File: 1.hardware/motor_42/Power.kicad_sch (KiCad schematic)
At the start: 0 parts

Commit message: 중간 저장
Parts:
- added C1: 10uF/50V, symbol Device:C_Small_US
- added C17, C18, C19, C20: CL31A106KBHNNNE, symbol Device:C_Small_US
- added C2, C3, C9: 0.1uF/50V, symbol Device:C_Small_US
- added C4, C5, C7, C8: 22uF/16V, symbol Device:C_Small_US
- added C6: 75pF/50V, symbol Device:C_Small_US
- added D1: SS54F-HF, SODFL4626X120N, symbol SamacSys_Parts:SS54F-HF
- added D2: SMBJ28CA-Q, DIONM5436X244N, symbol SamacSys_Parts:SMBJ28CA-Q
- added D3: B5819WS, SOD2613X100N, symbol SamacSys_Parts:B5819WS
- added H1, H2, H3, H4: MountingHole, symbol Mechanical:MountingHole
- added L1: 15uH, symbol Device:L
- added L2: 2.2uH, symbol Device:L
- added PS1: TPS563201DDCT, SOT95P280X110-6N, symbol SamacSys_Parts:TPS563201DDCT
- added R1: 100k/0.063w, symbol Device:R_Small_US
- added R2: 13.3k/0.063w, symbol Device:R_Small_US
- added R3: 511k/0.063w, symbol Device:R_Small_US
- added R4: 105k/0.063w, symbol Device:R_Small_US
- added R5: 49.9R/0.063w, symbol Device:R_Small_US
- added R6, R8: 10k/0.063w, symbol Device:R_Small_US
- added R7: 33.2k/0.063w, symbol Device:R_Small_US
- added U3: TPS54202DDC, Package_TO_SOT_SMD:SOT-23-6, symbol Regulator_Switching:TPS54202DDC
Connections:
- net GND: now also C1.2, C17.2, C18.2, C19.2, C2.2, C20.2, C4.2, C5.2, C7.2, C8.2, D2.2, PS1.1 (GND), R2.2, R4.2, R6.2, U3.1 (GND)
- net VCC: now also C17.1, C18.1, C19.1, C20.1, D1.1, D2.1, D3.2
- new net: C1.1, C2.1, D3.1, R3.1, U3.3 (VIN)
- new net: C3.2, L1.1, U3.2 (SW)
- new net: C9.2, L2.2, PS1.2 (SW)
- new net: PS1.4 (VFB), R6.1, R7.2
- new net: C9.1, PS1.6 (VBST)
- new net: R3.2, R4.1, U3.5 (EN)
- new net: C6.1, R1.1, R5.2
- new net: C6.2, R1.2, R2.1, U3.4 (FB)
- new net: PS1.5 (EN), R8.1
- new net: C3.1, U3.6 (BOOT)
- new net 3V3: C7.1, C8.1, L2.1, R7.1
- new net 5V: C4.1, C5.1, L1.2, PS1.3 (VIN), R5.1, R8.2
- new net VCC_IN: D1.2
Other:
- note added: "3V3"
- note added: "5V"

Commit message: 중간 저장
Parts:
- renumbered C17 to C1, C6 to C10, C9 to C11, C7 to C12, C8 to C13, C18 to C2, C19 to C3, C20 to C4, C3 to C5, C1 to C6, C2 to C7, C4 to C8, C5 to C9, R3 to R1, R5 to R2, R1 to R3, R2 to R5, R7 to R6, R8 to R7, R6 to R8, U3 to U1

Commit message: 회로도 대충 완성
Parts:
- removed D1: SS54F-HF, SODFL4626X120N, symbol SamacSys_Parts:SS54F-HF
- removed D2: SMBJ28CA-Q, DIONM5436X244N, symbol SamacSys_Parts:SMBJ28CA-Q
- added D2: SMBJ28CAQ-13-F, SamacSys_Parts:DIONM5336X250N, symbol SamacSys_Parts:SMBJ28CAQ-13-F
- added D5: SS54, PCM_Diode_SMD_AKL:D_SMC, symbol PCM_Diode_Schottky_AKL:SS54
- added J10: Conn_01x02, symbol Connector_Generic:Conn_01x02
- D3: footprint SOD2613X100N -> Diode_SMD:D_SOD-323
- H1, H2, H3, H4: footprint (none) -> MountingHole:MountingHole_3.2mm_M3
- R1: footprint (none) -> Resistor_SMD:R_0402_1005Metric
- R2: renamed from R4; footprint (none) -> Resistor_SMD:R_0402_1005Metric
- R3: renamed from R7; footprint (none) -> Resistor_SMD:R_0402_1005Metric
- R4: renamed from R6; footprint (none) -> Resistor_SMD:R_0402_1005Metric
- R5: renamed from R8; footprint (none) -> Resistor_SMD:R_0402_1005Metric
- R6: renamed from R2; footprint (none) -> Resistor_SMD:R_0402_1005Metric
- R7: renamed from R3; footprint (none) -> Resistor_SMD:R_0402_1005Metric
- R8: renamed from R5; footprint (none) -> Resistor_SMD:R_0402_1005Metric
- renumbered C12 to C1, C4 to C10, C8 to C11, C9 to C12, C10 to C13, C6 to C2, C13 to C3, C7 to C4, C11 to C5, C1 to C6, C2 to C7, C3 to C8, C5 to C9, L2 to L1, L1 to L2
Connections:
- net 5V: now also J10.1 (Pin_1)
- net GND: now also D2.2
- net VCC: now also D2.1, D5.1 (K)
- net VCC_IN: now also D5.2 (A)
- new net USB_VBUS: J10.2 (Pin_2)

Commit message: 수정
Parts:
- removed PS1: TPS563201DDCT, SOT95P280X110-6N, symbol SamacSys_Parts:TPS563201DDCT
- added C34, C35: 10uF/16V, Capacitor_SMD:C_0805_2012Metric, symbol Device:C_Small_US
- added C36: 0.1uF/50V, Capacitor_SMD:C_0402_1005Metric, symbol Device:C_Small_US
- added U7: TPS563203, Package_TO_SOT_SMD:SOT-563, symbol Regulator_Switching:TPS563203
- C1, C11, C12, C3: value 22uF/16V -> 22uF/10V; footprint (none) -> Capacitor_SMD:C_1206_3216Metric
- C10, C6, C7, C8: footprint (none) -> Capacitor_SMD:C_1206_3216Metric
- C13, C4, C5, C9: footprint (none) -> Capacitor_SMD:C_0402_1005Metric
- C2: value 10uF/50V -> CL31A106KBHNNNE; footprint (none) -> Capacitor_SMD:C_1206_3216Metric
- J10: value Conn_01x02 -> VBUS_EN; footprint (none) -> Connector_PinHeader_2.54mm:PinHeader_1x02_P2.54mm_Vertical
- L1: footprint (none) -> Inductor_SMD:L_Sunlord_SWPA252012S
- L2: footprint (none) -> Inductor_SMD:L_Sunlord_SWPA4020S
- R3: value 10k/0.063w -> 100k/0.063w
- R4: value 33.2k/0.063w -> 135k/0.063w
- R5: value 10k/0.063w -> 30k/0.063w
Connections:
- net 5V: now also R3.1, C34.1, C35.1, C36.1, U7.1 (VIN); no longer R3.2
- net GND: now also C34.2, C35.2, C36.2, U7.3 (GND)
- net at C5.2, L1.2: now also U7.2 (SW)
- net at R4.2, R5.1: now also U7.6 (FB)
- net at C5.1: now also U7.4 (BST)
- new net: R3.2, U7.5 (EN)
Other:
- moved on the sheet: C1, C3, C5, L1, R3, R4, R5

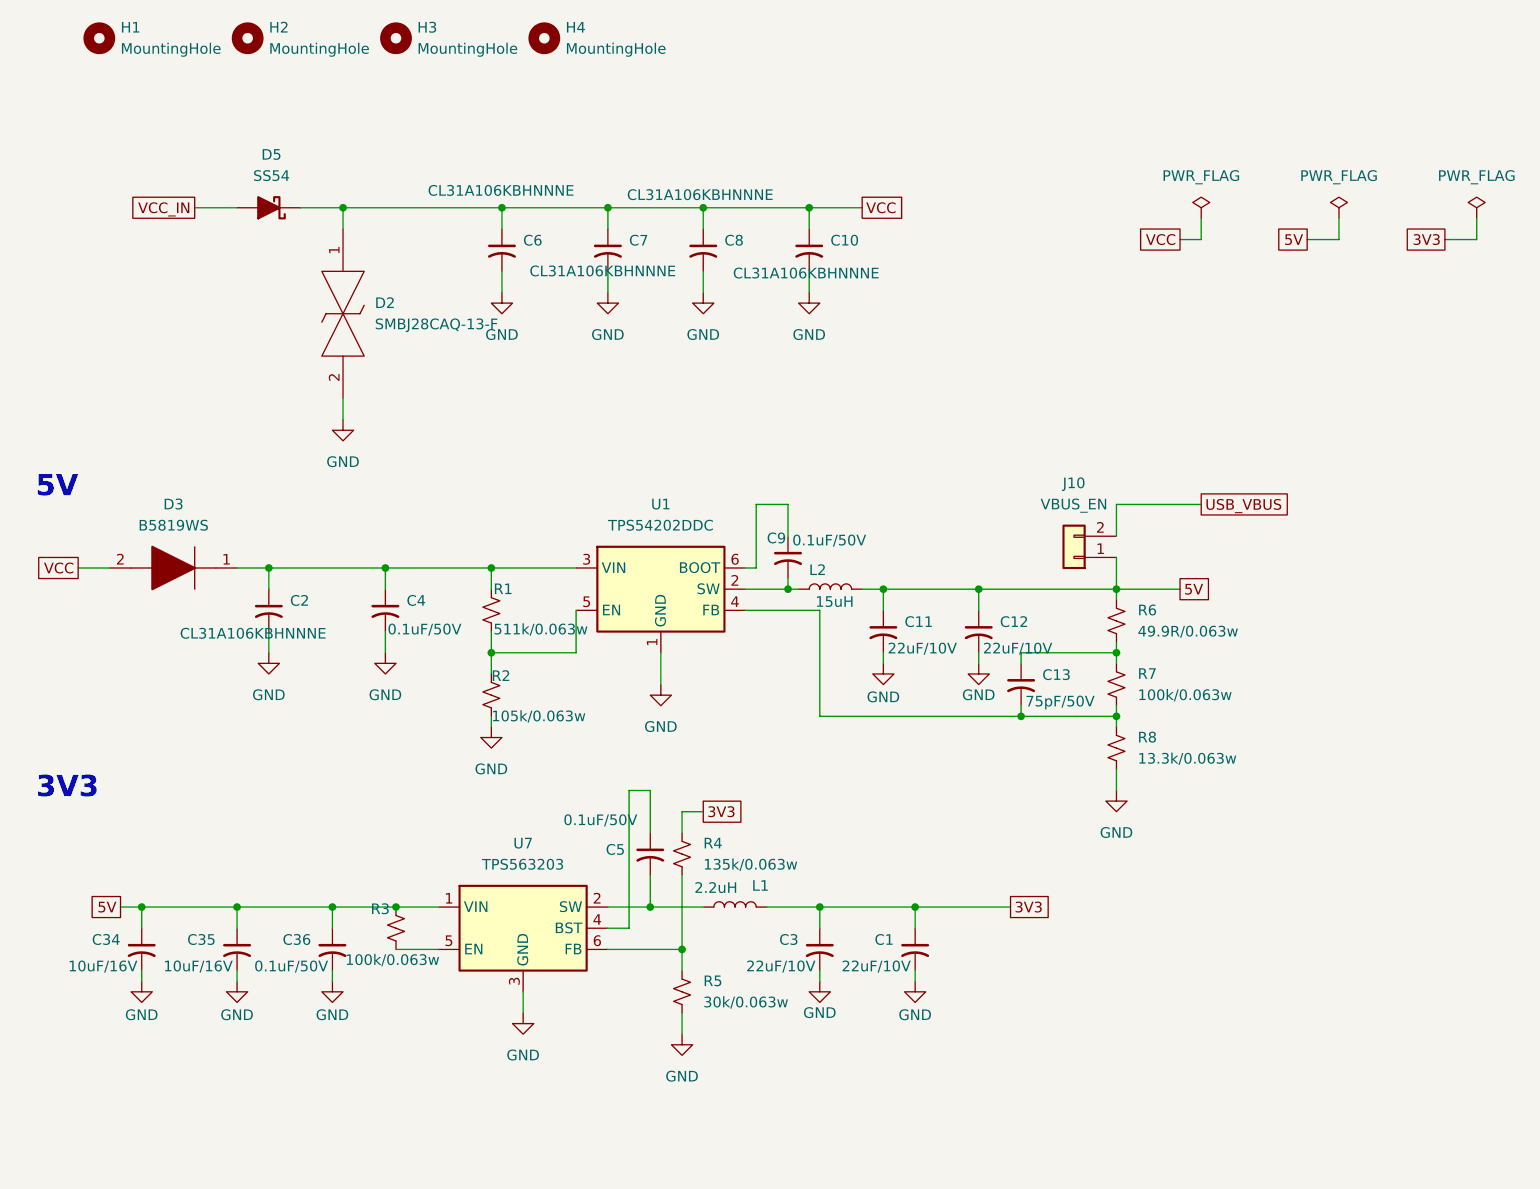
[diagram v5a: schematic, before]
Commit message: 3V3 LDO변경 및 대략적 위치 세팅
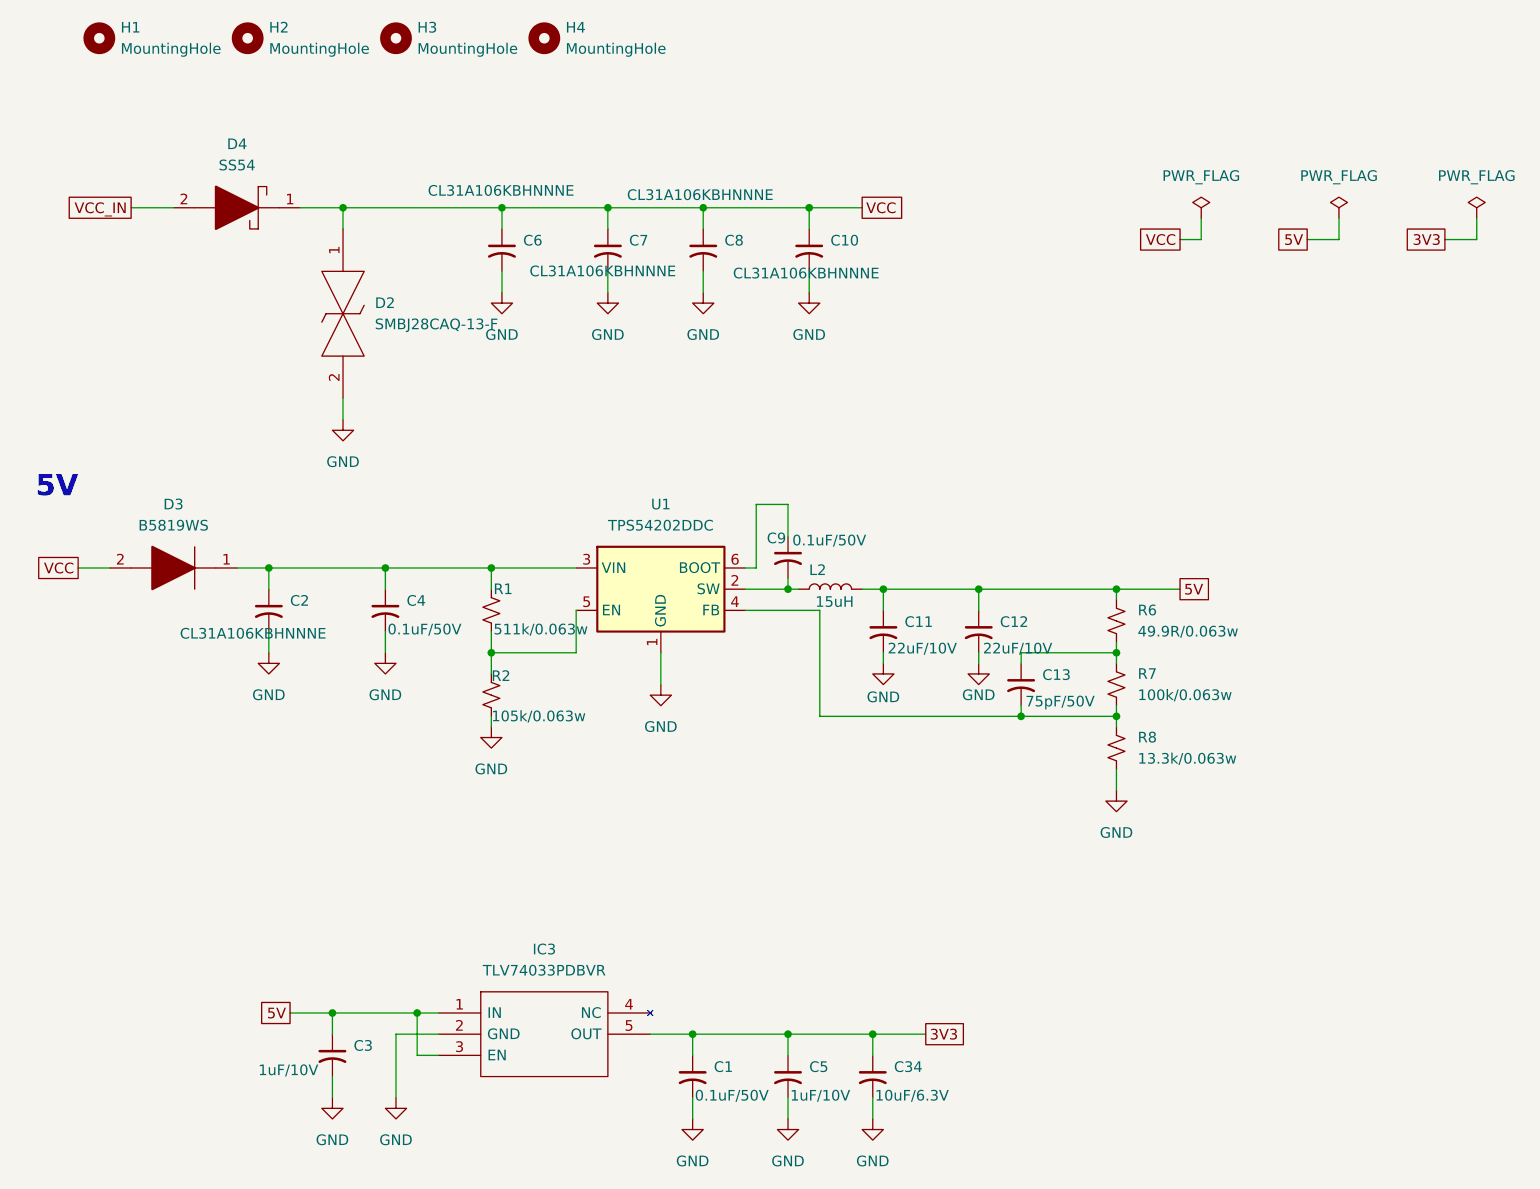
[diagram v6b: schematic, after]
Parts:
- removed C35: 10uF/16V, Capacitor_SMD:C_0805_2012Metric, symbol Device:C_Small_US
- removed C36: 0.1uF/50V, Capacitor_SMD:C_0402_1005Metric, symbol Device:C_Small_US
- removed D5: SS54, PCM_Diode_SMD_AKL:D_SMC, symbol PCM_Diode_Schottky_AKL:SS54
- removed J10: VBUS_EN, Connector_PinHeader_2.54mm:PinHeader_1x02_P2.54mm_Vertical, symbol Connector_Generic:Conn_01x02
- removed L1: 2.2uH, Inductor_SMD:L_Sunlord_SWPA252012S, symbol Device:L
- removed R3: 100k/0.063w, Resistor_SMD:R_0402_1005Metric, symbol Device:R_Small_US
- removed R4: 135k/0.063w, Resistor_SMD:R_0402_1005Metric, symbol Device:R_Small_US
- removed R5: 30k/0.063w, Resistor_SMD:R_0402_1005Metric, symbol Device:R_Small_US
- removed U7: TPS563203, Package_TO_SOT_SMD:SOT-563, symbol Regulator_Switching:TPS563203
- added D4: SS54, SamacSys_Parts:DIOM5126X245N, symbol SamacSys_Parts:SS54
- added IC3: TLV74033PDBVR, SamacSys_Parts:SOT95P280X145-5N, symbol SamacSys_Parts:TLV74033PDBVR
- C1: value 22uF/10V -> 0.1uF/50V; footprint Capacitor_SMD:C_1206_3216Metric -> Capacitor_SMD:C_0402_1005Metric
- C3: value 22uF/10V -> 1uF/10V; footprint Capacitor_SMD:C_1206_3216Metric -> Capacitor_SMD:C_0402_1005Metric
- C34: value 10uF/16V -> 10uF/6.3V; footprint Capacitor_SMD:C_0805_2012Metric -> Capacitor_SMD:C_0603_1608Metric
- C5: value 0.1uF/50V -> 1uF/10V
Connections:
- net 3V3: now also C34.1, C5.1, IC3.5 (OUT); no longer C3.1
- net 5V: now also C3.1, IC3.1 (IN), IC3.3 (EN); no longer C34.1
- net GND: now also C5.2, IC3.2 (GND)
- net VCC: now also D4.1
- net VCC_IN: now also D4.2
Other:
- note removed: "3V3"

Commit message: 얼추 다 그림
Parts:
- removed C1: 0.1uF/50V, Capacitor_SMD:C_0402_1005Metric, symbol Device:C_Small_US
- removed C3, C5: 1uF/10V, Capacitor_SMD:C_0402_1005Metric, symbol Device:C_Small_US
- removed C34: 10uF/6.3V, Capacitor_SMD:C_0603_1608Metric, symbol Device:C_Small_US
- removed IC3: TLV74033PDBVR, SamacSys_Parts:SOT95P280X145-5N, symbol SamacSys_Parts:TLV74033PDBVR
- L2: value 15uH -> 10uH
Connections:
- net 3V3: now also C11.1, C12.1, L2.2, R6.1
- net 5V: no longer C11.1, C12.1, L2.2, R6.1
